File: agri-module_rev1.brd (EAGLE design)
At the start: 160 x 100 mm, 0 parts

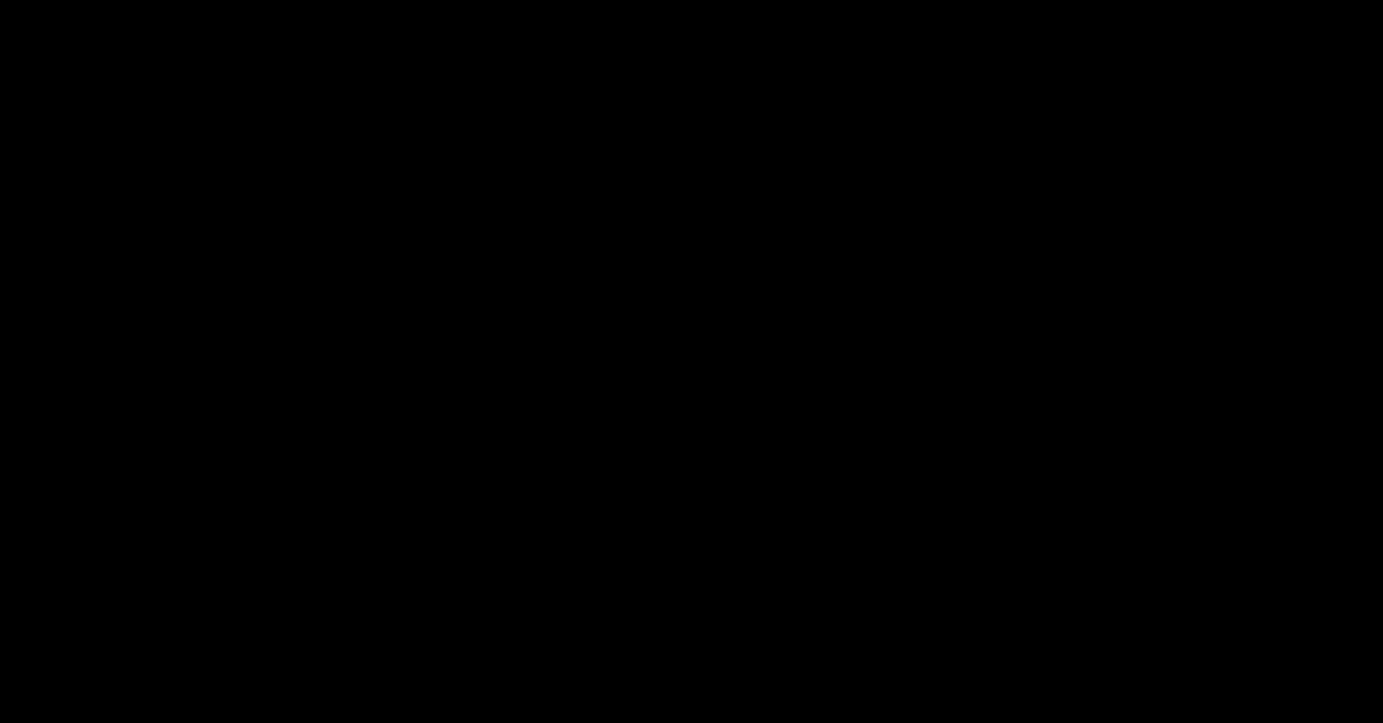
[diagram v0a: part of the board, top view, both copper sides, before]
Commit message: add ISL and new RJ45 pinout
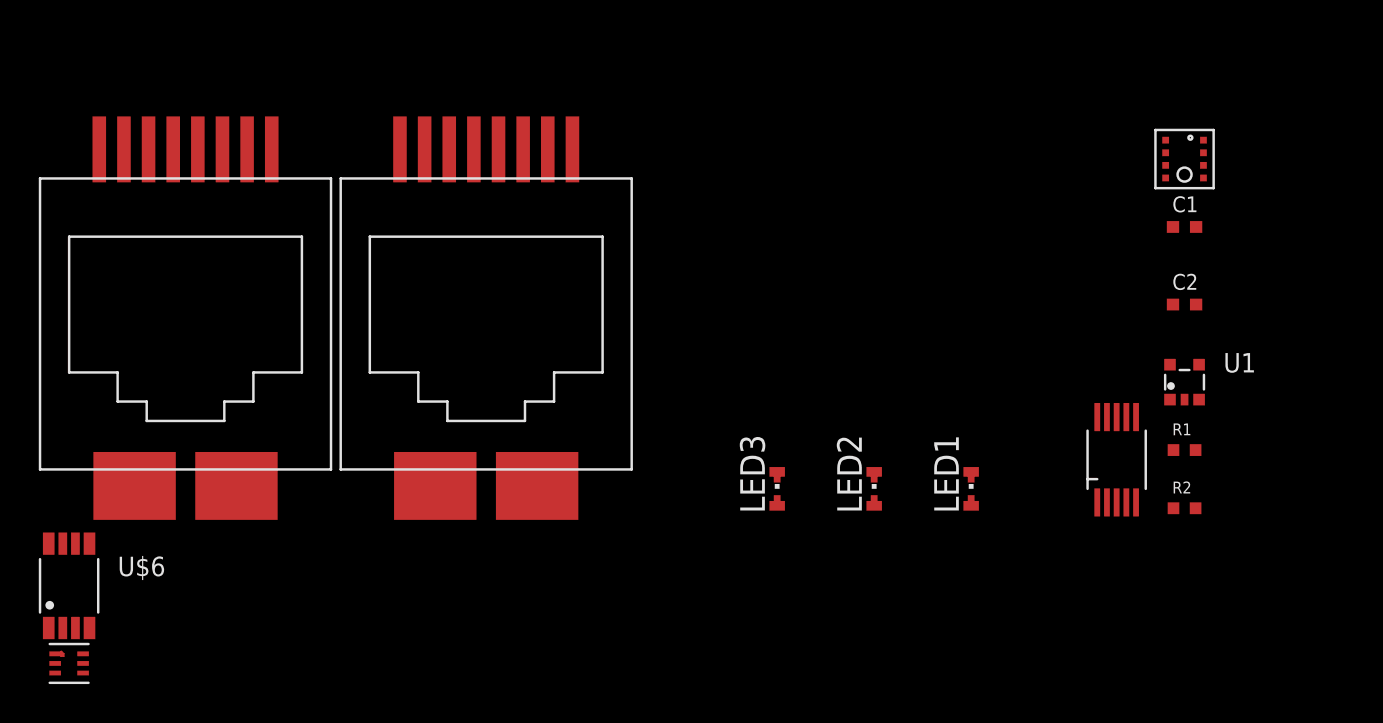
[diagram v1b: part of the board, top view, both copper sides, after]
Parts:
- added C1, C2: 100nF, BrainGrid - Capacitors:C0402-BG
- added LED1, LED2, LED3: (no value), BrainGrid - Diodes:CHIPLED-0603-TTW
- added R1, R2: 1.8k, BrainGrid - Resistors:R0402-BG
- added U$1: RJ45_RA_SMD, BrainGrid - Electromechanical:RJ45_RA_SMD
- added U$2: RJ45_OUT_AGRI-BRD, BrainGrid - Electromechanical:RJ45_RA_SMD
- added U$3: BME280, BrainGrid - Sensors:BME280
- added U$4: ADS1015, BrainGrid - Analog:ADS1015
- added U$5: ISL29125_RGB_SENSE, BrainGrid - Sensors:ISL29125_RGB_SENSE
- added U$6: PCA9540B_I2C_SWITCH, NXP:SOT505-1
- added U1: 74HC1G79GW, NXP:SOT353-1
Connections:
- new net 3.6V_HP: C1.1, C2.1, R1.2, R2.2, U$1.2, U$3.P2, U$3.P6, U$3.P8, U$4.1, U$4.8, U$6.3
- new net 5V: U$1.1, U$2.8
- new net GND: LED1.C@1, LED2.C@1, LED3.C@1, U$1.8, U$2.1, U$3.P1, U$4.3, U$6.6, U1.3
- new net N$1: R1.1, U$3.P3
- new net N$10: U$1.7
- new net N$11: U$1.4, U$6.2
- new net N$12: U$3.P5, U$4.9, U$5.4, U$6.4
- new net N$13: U$3.P4, U$4.10, U$5.6, U$6.5
- new net N$14: C1.2, C2.2, U$3.P7
- new net N$2: R2.1
- new net N$3: U$1.6, U$6.1
- new net N$4: U$4.4
- new net N$5: LED3.A@1, U$4.5
- new net N$6: LED2.A@1, U$4.6
- new net N$7: LED1.A@1, U$4.7
- new net N$8: U$6.8
- new net N$9: U$6.7
- new net VCC: U1.5

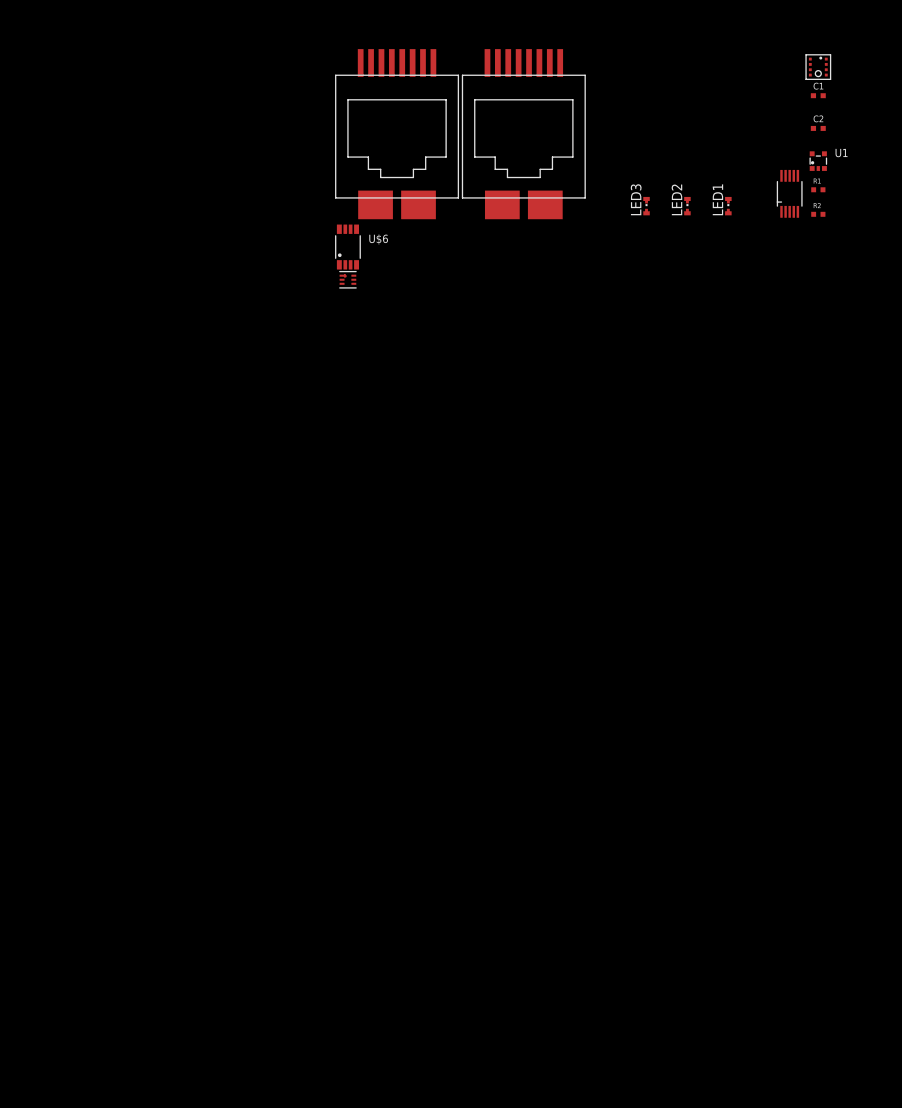
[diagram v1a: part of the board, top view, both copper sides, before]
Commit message: Everything wired up, not looked over yet
-replaced ISL with RGB gesture
-added hot film amp and CO2 amp
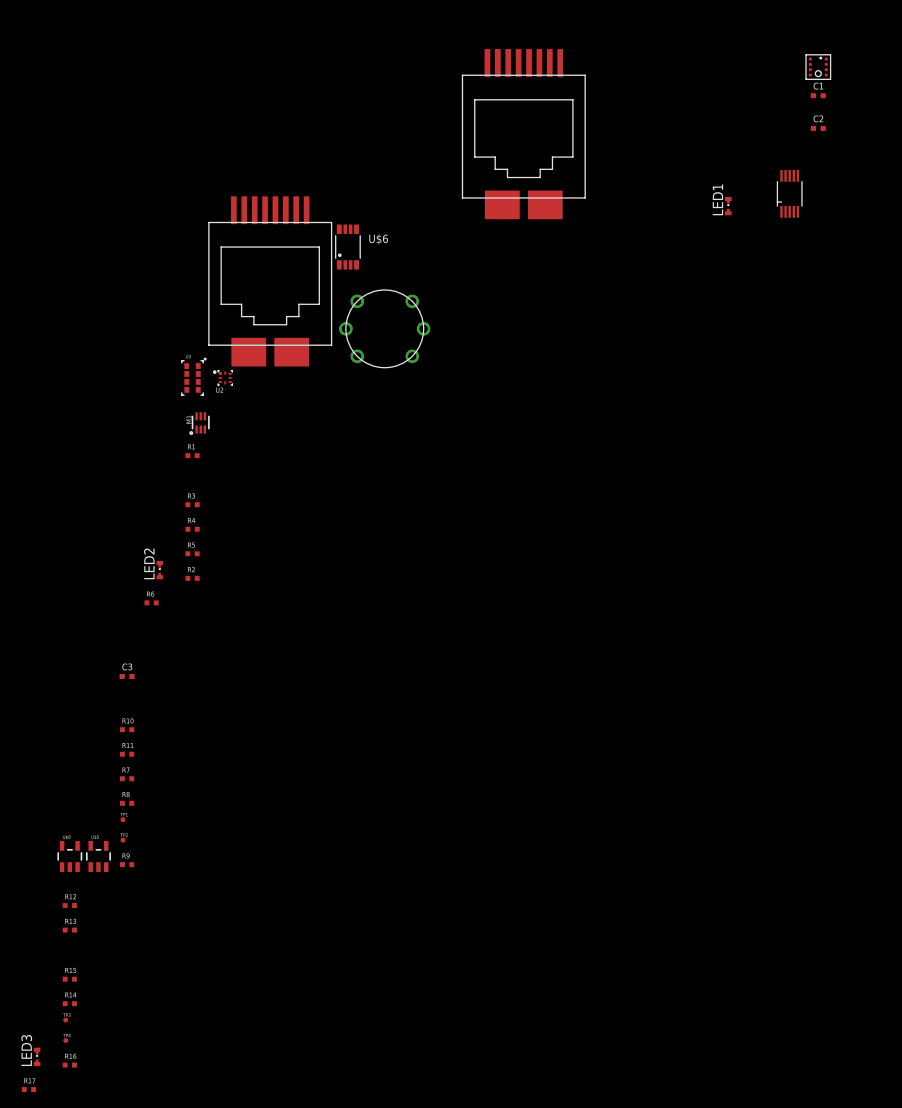
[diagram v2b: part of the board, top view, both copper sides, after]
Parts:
- removed U1: 74HC1G79GW, NXP:SOT353-1
- added C3: 100nF, BrainGrid - Capacitors:C0402-BG
- added M1: DMG1023, BrainGrid - Transistors:SOT666
- added R10, R16, R17: 0R, BrainGrid - Resistors:R0402-BG
- added R11, R7: 1k, BrainGrid - Resistors:R0402-BG
- added R12, R13, R14, R15: 100R, BrainGrid - Resistors:R0402-BG
- added R3, R4, R5, R6: 10k, BrainGrid - Resistors:R0402-BG
- added R8: 5.1k, BrainGrid - Resistors:R0402-BG
- added R9: 100k, BrainGrid - Resistors:R0402-BG
- added TP1, TP2, TP3, TP4: TEST_PAD, BrainGrid - Electromechanical:TP06R
- added U$7: MG811, BrainGrid - Sensors:MG811
- added U$8: MCP6001T, SparkFun-AnalogIC:SOT23-5
- added U2: PCA9570, BrainGrid - MAC-PHY-Glue:XQFN8
- added U3: APDS-9960, BrainGrid - Sensors:APDS-9960
- R1: value 1.8k -> 100R
- R2: value 1.8k -> 10k
- U$2: value RJ45_OUT_AGRI-BRD -> RJ45_RA_SMD
- U$5: value ISL29125_RGB_SENSE -> MCP6001T; device BrainGrid - Sensors:ISL29125_RGB_SENSE -> SparkFun-AnalogIC:SOT23-5
- moved LED3 127.9 mm to (-125.0, -123.0)
- moved R2 88.5 mm to (-106.0, -64.5)
- moved R1 83.1 mm to (-106.0, -49.5)
- moved LED2 78.4 mm to (-110.0, -63.5)
- moved U$5 76.8 mm to (-117.5, -98.5)
- moved U$2 23.8 mm to (-96.5, -28.5)
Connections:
- removed net N$5 (its old number): LED3.A@1, U$4.5
- new net CO2_POW: M1.6, R16.2, U$7.H1
- new net EC_POW: TP2.TP, U2.6
- new net GEST_LED: R1.2, U2.4
- new net N$15: R5.1, U$1.6, U$6.1, U2.7
- new net N$16: R7.2, R8.2, U$4.5, U$5.1
- new net N$17: R10.2, U$7.H2
- new net N$18: M1.2, U2.3
- new net N$19: C3.1, R7.1
- new net N$20: R13.2, U$8.4
- new net N$21: R12.2, R14.2, R15.1, TP3.TP, U$8.3
- new net N$22: R14.1, TP4.TP, U$8.1
- new net N$23: R15.2, R16.1, U$8.5
- new net N$24: LED3.A@1, R17.2, U$4.4
- new net N$7: U$2.4, U$6.7
- new net T_SENSE: U$1.5, U$2.5
- net 3.6V_HP: now also M1.4, R3.2, R4.2, R5.2, U$1.3, U$2.3, U$5.5, U2.1; no longer C1.1, C2.1, R1.2, U$1.2, U$3.P2, U$3.P6, U$3.P8, U$4.1, U$4.8, U$6.3
- net 5V: now also M1.1, U$1.2, U$2.1, U$2.2; no longer U$2.8
- net GND: now also C1.2, C2.2, R10.1, R11.1, R12.1, R13.1, R9.1, U$1.7, U$2.7, U$2.8, U$3.P5, U$3.P7, U$4.1, U$4.2, U$7.A1, U$7.A2, U$8.2, U2.5, U3.6; no longer LED3.C@1, U$2.1, U1.3
- net N$1: now also M1.5, U2.2; no longer R1.1, U$3.P3
- net N$10: now also R6.1, U3.2; no longer U$1.7
- net N$11: now also R3.1, U$3.P3, U$4.9, U$6.4, U3.1; no longer U$1.4, U$6.2
- net N$12: now also LED3.C@1, R17.1, R9.2, TP1.TP; no longer U$3.P5, U$4.9, U$5.4, U$6.4
- net N$13: now also C3.2, R11.2, R8.1, U$5.2, U$5.4; no longer U$3.P4, U$4.10, U$5.6, U$6.5
- net N$14: now also R4.1, U$1.4, U$6.2, U2.8; no longer C1.2, C2.2, U$3.P7
- net N$2: now also U3.3, U3.4; no longer R2.1
- net N$3: now also R2.1, U$3.P4, U$4.10, U$6.5, U3.7; no longer U$1.6, U$6.1
- net N$4: now also R1.1, U3.5; no longer U$4.4
- net N$8: now also U$2.6
- net N$9: now also U$5.3, U$7.B1, U$7.B2; no longer U$6.7
- net VCC: now also C1.1, C2.1, M1.3, R6.2, U$3.P2, U$3.P6, U$3.P8, U$4.8, U$6.3, U3.8; no longer U1.5
